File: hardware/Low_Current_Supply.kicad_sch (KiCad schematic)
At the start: 19 parts, among them U5001 TPS62160DSG, U5002 TPS73633DBVR

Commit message: feat(schematic): refactor main heirarchy
This commit makes a bunch of changes to how power is delivered on the
schematic. It also adds the probit header and the i2c output connector
on the main page of the schematic. Lastly, it changes it so that USB
power should work and also not power the 5V rail to the mosfet ICs.
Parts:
- added D5003: FIX ME PLEASE I BEG OF YOU, symbol Device:D
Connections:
- net at C5002.1, L5001.2, R5001.2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: now also D5003.2 (A); no longer C5003.1, R5003.1, TP5003.1, U5002.1 (IN), U5002.3 (EN)
- net 3.3V renamed +3.3V
- new net VBUS: C5003.1, D5003.1 (K), R5003.1, TP5003.1, U5002.1 (IN), U5002.3 (EN)
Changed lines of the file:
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@@
 	(paper "A4")
 	(junction
+		(at 144.78 71.12)
+		(diameter 0)
+		(color 0 0 0 0)
+	)
+	(junction
 		(at 191.77 113.03)
 		(diameter 0)
@@
 	)
 	(junction
+		(at 158.75 100.33)
+		(diameter 0)
+		(color 0 0 0 0)
+	)
+	(junction
+		(at 119.38 71.12)
+		(diameter 0)
+		(color 0 0 0 0)
+	)
+	(junction
+		(at 96.52 90.17)
+		(diameter 0)
+		(color 0 0 0 0)
+	)
+	(junction
+		(at 245.11 95.25)
+		(diameter 0)
+		(color 0 0 0 0)
+	)
+	(junction
+		(at 222.25 71.12)
+		(diameter 0)
+		(color 0 0 0 0)
+	)
+	(junction
+		(at 132.08 71.12)
+		(diameter 0)
+		(color 0 0 0 0)
+	)
+	(junction
+		(at 71.12 71.12)
+		(diameter 0)
+		(color 0 0 0 0)
+	)
+	(junction
+		(at 91.44 90.17)
+		(diameter 0)
+		(color 0 0 0 0)
+	)
+	(junction
+		(at 237.49 95.25)
+		(diameter 0)
+		(color 0 0 0 0)
+	)
+	(junction
+		(at 109.22 90.17)
+		(diameter 0)
+		(color 0 0 0 0)
+	)
+	(junction
+		(at 158.75 95.25)
+		(diameter 0)
+		(color 0 0 0 0)
+	)
+	(junction
+		(at 78.74 71.12)
+		(diameter 0)
+		(color 0 0 0 0)
+	)
+	(junction
 		(at 158.75 71.12)
 		(diameter 0)
@@
 	)
 	(junction
-		(at 158.75 100.33)
-		(diameter 0)
-		(color 0 0 0 0)
-	)
-	(junction
-		(at 119.38 71.12)
-		(diameter 0)
-		(color 0 0 0 0)
-	)
-	(junction
-		(at 96.52 90.17)
-		(diameter 0)
-		(color 0 0 0 0)
-	)
-	(junction
-		(at 245.11 95.25)
-		(diameter 0)
-		(color 0 0 0 0)
-	)
-	(junction
-		(at 222.25 71.12)
-		(diameter 0)
-		(color 0 0 0 0)
-	)
-	(junction
-		(at 132.08 71.12)
-		(diameter 0)
-		(color 0 0 0 0)
-	)
-	(junction
-		(at 71.12 71.12)
-		(diameter 0)
-		(color 0 0 0 0)
-	)
-	(junction
-		(at 91.44 90.17)
-		(diameter 0)
-		(color 0 0 0 0)
-	)
-	(junction
-		(at 237.49 95.25)
-		(diameter 0)
-		(color 0 0 0 0)
-	)
-	(junction
-		(at 109.22 90.17)
-		(diameter 0)
-		(color 0 0 0 0)
-	)
-	(junction
-		(at 158.75 95.25)
-		(diameter 0)
-		(color 0 0 0 0)
-	)
-	(junction
-		(at 78.74 71.12)
-		(diameter 0)
-		(color 0 0 0 0)
-	)
-	(junction
 		(at 194.31 71.12)
 		(diameter 0)
@@
 	)
 	(junction
-		(at 144.78 71.12)
-		(diameter 0)
-		(color 0 0 0 0)
-	)
-	(junction
 		(at 261.62 95.25)
 		(diameter 0)
@@
 	(wire
 		(pts
-			(xy 144.78 71.12) (xy 158.75 71.12)
-		)
-		(stroke
-			(width 0)
-			(type default)
-		)
-	)
-	(wire
-		(pts
 			(xy 237.49 95.25) (xy 245.11 95.25)
 		)
@@
 	(wire
 		(pts
+			(xy 144.78 71.12) (xy 147.32 71.12)
+		)
+		(stroke
+			(width 0)
+			(type default)
+		)
+	)
+	(wire
+		(pts
 			(xy 222.25 71.12) (xy 270.51 71.12)
 		)
@@
 	(wire
 		(pts
+			(xy 158.75 62.23) (xy 158.75 71.12)
+		)
+		(stroke
+			(width 0)
+			(type default)
+		)
+	)
+	(wire
+		(pts
 			(xy 223.52 95.25) (xy 228.6 95.25)
 		)
@@
 	(wire
 		(pts
+			(xy 154.94 71.12) (xy 158.75 71.12)
+		)
+		(stroke
+			(width 0)
+			(type default)
+		)
+	)
+	(wire
+		(pts
 			(xy 91.44 90.17) (xy 91.44 88.9)
 		)
@@
 		)
 	)
-	(global_label "5V"
+	(hierarchical_label "VBUS"
 		(shape input)
-		(at 270.51 71.12 0)
-		(fields_autoplaced yes)
+		(at 158.75 62.23 180)
 		(effects
 			(font
 				(size 1.27 1.27)
 			)
-			(justify left)
-		)
-		(property "Intersheetrefs" "${INTERSHEET_REFS}"
-			(at 275.7933 71.12 0)
-			(effects
-				(font
-					(size 1.27 1.27)
-				)
-				(justify left)
-				(hide yes)
-			)
-		)
-	)
-	(global_label "12V"
+			(justify right)
+		)
+	)
+	(hierarchical_label "12V"
 		(shape input)
 		(at 46.99 71.12 180)
-		(fields_autoplaced yes)
 		(effects
 			(font
@@
 			(justify right)
 		)
-		(property "Intersheetrefs" "${INTERSHEET_REFS}"
-			(at 40.4972 71.12 0)
-			(effects
-				(font
-					(size 1.27 1.27)
-				)
-				(justify right)
-				(hide yes)
-			)
-		)
-	)
-	(global_label "3.3V"
-		(shape input)
+	)
+	(hierarchical_label "+3.3V"
+		(shape output)
 		(at 269.24 95.25 0)
-		(fields_autoplaced yes)
 		(effects
 			(font
@@
 			(justify left)
 		)
-		(property "Intersheetrefs" "${INTERSHEET_REFS}"
-			(at 276.3376 95.25 0)
-			(effects
-				(font
-					(size 1.27 1.27)
-				)
-				(justify left)
-				(hide yes)
-			)
+	)
+	(hierarchical_label "5V"
+		(shape output)
+		(at 270.51 71.12 0)
+		(effects
+			(font
+				(size 1.27 1.27)
+			)
+			(justify left)
 		)
 	)
@@
 					(unit 1)
 				)
+			)
+		)
+	)
+	(symbol
+		(lib_id "Device:D")
+		(at 151.13 71.12 180)
+		(unit 1)
+		(exclude_from_sim no)
+		(in_bom yes)
+		(on_board yes)
+		(dnp no)
+		(fields_autoplaced yes)
+		(property "Reference" "D5003"
+			(at 151.13 64.77 0)
+			(effects
+				(font
+					(size 1.27 1.27)
+				)
+			)
+		)
+		(property "Value" "FIX ME PLEASE I BEG OF YOU"
+			(at 151.13 67.31 0)
+			(effects
+				(font
+					(size 1.27 1.27)
+				)
+			)
+		)
+		(property "Footprint" ""
+			(at 151.13 71.12 0)
+			(effects
+				(font
+					(size 1.27 1.27)
+				)
+				(hide yes)
+			)
+		)
+		(property "Datasheet" "~"
+			(at 151.13 71.12 0)
+			(effects
+				(font
+					(size 1.27 1.27)
+				)
+				(hide yes)
+			)
+		)
+		(property "Description" "Diode"
+			(at 151.13 71.12 0)
+			(effects
+				(font
+					(size 1.27 1.27)
+				)
+				(hide yes)
+			)
+		)
+		(property "Sim.Device" "D"
+			(at 151.13 71.12 0)
+			(effects
+				(font
+					(size 1.27 1.27)
+				)
+				(hide yes)
+			)
+		)
+		(property "Sim.Pins" "1=K 2=A"
+			(at 151.13 71.12 0)
+			(effects
+				(font
+					(size 1.27 1.27)
+				)
+				(hide yes)
+			)
+		)
+		(pin "1"
+		)
+		(pin "2"
+		)
+		(instances
+			(project ""
+				(path "/d5303413-7068-41ba-88e3-39dfa38d31b7/c1da4524-645b-40e4-93f8-f7b345299022"
+					(reference "D5003")
+					(unit 1)
+				)

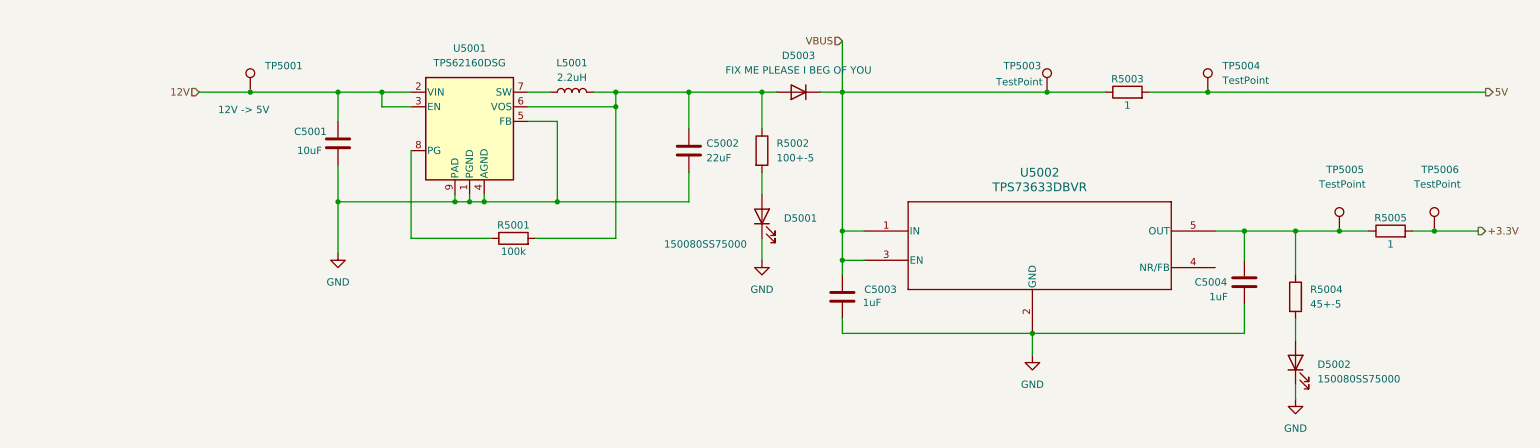
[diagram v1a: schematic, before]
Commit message: feat: fix pcb changes for 12V and low current supply
Swapped 5V regulator, added diodes, fixed connectors and general
placement. Changes to complete list for 12V and low current supply.
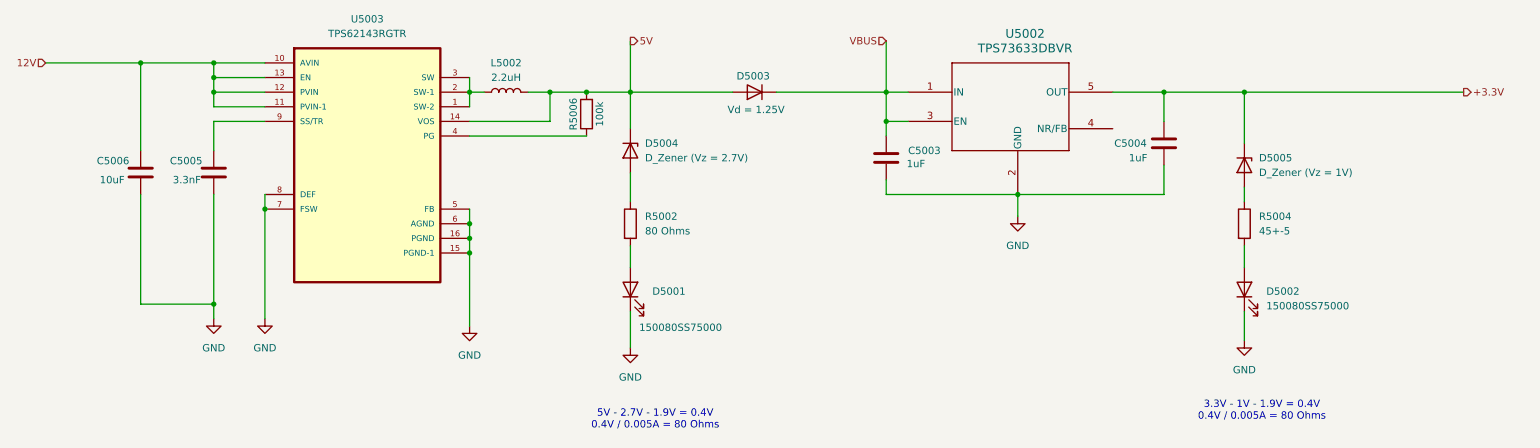
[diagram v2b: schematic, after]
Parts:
- removed C5001: 10uF, Capacitor_SMD:C_0805_2012Metric_Pad1.18x1.45mm_HandSolder, symbol Device:C
- removed C5002: 22uF, Capacitor_SMD:C_0805_2012Metric, symbol Device:C
- removed L5001: 2.2uH, Inductor_SMD:L_0805_2012Metric_Pad1.15x1.40mm_HandSolder, symbol Device:L
- removed R5001: 100k, Resistor_SMD:R_0805_2012Metric, symbol Device:R
- removed R5003, R5005: 1, Resistor_SMD:R_0805_2012Metric, symbol Device:R
- removed TP5001: 12V -> 5V, TestPoint:TestPoint_Pad_1.5x1.5mm, symbol Connector:TestPoint
- removed TP5003, TP5004, TP5005, TP5006: TestPoint, TestPoint:TestPoint_Pad_1.5x1.5mm, symbol Connector:TestPoint
- removed U5001: TPS62160DSG, Package_SON:WSON-8-1EP_2x2mm_P0.5mm_EP0.9x1.6mm_ThermalVias, symbol Regulator_Switching:TPS62160DSG
- added C5005: 3.3nF, Capacitor_SMD:C_0805_2012Metric_Pad1.18x1.45mm_HandSolder, symbol Device:C
- added C5006: 10uF, Capacitor_SMD:C_0805_2012Metric_Pad1.18x1.45mm_HandSolder, symbol Device:C
- added D5004: D_Zener (Vz = 2.7V), work:SOD123_DIO, symbol Device:D_Zener
- added D5005: D_Zener (Vz = 1V), work:P25_DO-214AC_SMA, symbol Device:D_Zener
- added L5002: 2.2uH, Inductor_SMD:L_0805_2012Metric_Pad1.15x1.40mm_HandSolder, symbol Device:L
- added R5006: 100k, Resistor_SMD:R_0805_2012Metric, symbol Device:R
- added U5003: TPS62143RGTR, TPS62143RGTR:QFN50P300X300X100-17N, symbol TPS62143RGTR:TPS62143RGTR
- D5003: value FIX ME PLEASE I BEG OF YOU -> Vd = 1.25V; footprint (none) -> work:SOD123_DIO
- R5002: value 100+-5 -> 80 Ohms
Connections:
- net +3.3V: now also C5004.1, U5002.5 (OUT), D5005.1 (K)
- net 12V: now also C5006.1, U5003.10 (AVIN), U5003.11 (PVIN-1), U5003.12 (PVIN), U5003.13 (EN)
- net 5V: now also D5003.2 (A), D5004.1 (K), L5002.2, R5006.2, U5003.14 (VOS)
- net GND: now also C5005.2, C5006.2, U5003.15 (PGND-1), U5003.16 (PGND), U5003.5 (FB), U5003.6 (AGND), U5003.7 (FSW), U5003.8 (DEF)
- net at R5002.1: now also D5004.2 (A); no longer D5003.2 (A)
- new net: L5002.1, U5003.1 (SW-2), U5003.2 (SW-1), U5003.3 (SW)
- new net: R5006.1, U5003.4 (PG)
- new net: C5005.1, U5003.9 (SS/TR)
- new net: D5005.2 (A), R5004.1
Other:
- note added: "3.3V - 1V - 1.9V = 0.4V 0.4V / 0.005A = 80 Ohms"
- note added: "5V - 2.7V - 1.9V = 0.4V 0.4V / 0.005A = 80 Ohms"
- moved on the sheet: C5003, C5004, D5001, D5002, D5003, R5002, R5004, U5002

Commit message: feat(schematic): added cooler mounting holes
added cooler mounting holes to schematic
changed temp pins to read proper tempurature
small fixes
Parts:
- C5003, C5004: footprint Capacitor_SMD:C_0805_2012Metric -> Capacitor_SMD:C_0402_1005Metric
- C5005: footprint Capacitor_SMD:C_0805_2012Metric_Pad1.18x1.45mm_HandSolder -> Capacitor_SMD:C_0402_1005Metric
- C5006: footprint Capacitor_SMD:C_0805_2012Metric_Pad1.18x1.45mm_HandSolder -> Capacitor_SMD:C_0603_1608Metric
- D5001, D5002: footprint LED_SMD:LED_0805_2012Metric_Pad1.15x1.40mm_HandSolder -> LED_SMD:LED_0603_1608Metric
- L5002: footprint Inductor_SMD:L_0805_2012Metric_Pad1.15x1.40mm_HandSolder -> work:IND-SMD_L7.2-W6.6_GPSR07X0
- R5002: value 80 Ohms -> 82
- R5004: value 45+-5 -> 82
- R5006: footprint Resistor_SMD:R_0805_2012Metric -> Resistor_SMD:R_0402_1005Metric
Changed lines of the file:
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@@
 		(shape input)
 		(at 166.37 62.23 180)
-		(fields_autoplaced yes)
 		(effects
 			(font
@@
 		(shape input)
 		(at 20.32 66.04 180)
-		(fields_autoplaced yes)
 		(effects
 			(font
@@
 		(shape output)
 		(at 266.7 71.12 0)
-		(fields_autoplaced yes)
 		(effects
 			(font
@@
 		(shape output)
 		(at 121.92 62.23 0)
-		(fields_autoplaced yes)
 		(effects
 			(font
@@
 			)
 		)
-		(property "Datasheet" ""
+		(property "Datasheet" "https://jlcpcb.com/partdetail/TexasInstruments-TPS62143RGTR/C2070702"
 			(at 76.2 83.82 0)
 			(effects
@@
 			)
 		)
-		(property "Footprint" "LED_SMD:LED_0805_2012Metric_Pad1.15x1.40mm_HandSolder"
+		(property "Footprint" "LED_SMD:LED_0603_1608Metric"
 			(at 228.6 105.41 0)
 			(effects
@@
 			)
 		)
-		(property "Datasheet" "~"
+		(property "Datasheet" "https://jlcpcb.com/partdetail/Hubei_KentoElec-KT0603R/C2286"
 			(at 228.6 105.41 0)
 			(effects
@@
 			)
 		)
-		(property "Value" "80 Ohms"
+		(property "Value" "82"
 			(at 124.46 95.2499 0)
 			(effects
@@
 			)
 		)
-		(property "Datasheet" "~"
+		(property "Datasheet" "https://jlcpcb.com/partdetail/18529-0805W8F820JT5E/C17841"
 			(at 121.92 93.98 0)
 			(effects
@@
 			)
 		)
-		(property "Footprint" "Capacitor_SMD:C_0805_2012Metric_Pad1.18x1.45mm_HandSolder"
+		(property "Footprint" "Capacitor_SMD:C_0402_1005Metric"
 			(at 50.4952 88.9 0)
 			(effects
@@
 			)
 		)
-		(property "Datasheet" "~"
+		(property "Datasheet" "https://jlcpcb.com/partdetail/1888-0402B332K500NT/C1536"
 			(at 49.53 85.09 0)
 			(effects
@@
 			)
 		)
-		(property "Datasheet" "TPS73633DBVR"
+		(property "Datasheet" "https://jlcpcb.com/partdetail/TexasInstruments-TPS73633DBVR/C28038"
 			(at 160.02 71.12 0)
 			(effects
@@
 			)
 		)
-		(property "Footprint" "Capacitor_SMD:C_0805_2012Metric"
+		(property "Footprint" "Capacitor_SMD:C_0402_1005Metric"
 			(at 167.3352 86.36 0)
 			(effects
@@
 			)
 		)
-		(property "Datasheet" "~"
+		(property "Datasheet" "https://jlcpcb.com/partdetail/15107-CL05A105KP5NNNC/C14445"
 			(at 166.37 82.55 0)
 			(effects
@@
 			)
 		)
-		(property "Footprint" "Resistor_SMD:R_0805_2012Metric"
+		(property "Footprint" "Resistor_SMD:R_0402_1005Metric"
 			(at 116.078 74.93 90)
 			(effects
@@
 			)
 		)
-		(property "Datasheet" "~"
+		(property "Datasheet" "https://jlcpcb.com/partdetail/26484-0402WGF1003TCE/C25741"
 			(at 114.3 74.93 0)
 			(effects
@@
 			)
 		)
-		(property "Value" "45+-5"
+		(property "Value" "82"
 			(at 231.14 95.2499 0)
 			(effects
@@
 			)
 		)
-		(property "Datasheet" "~"
+		(property "Datasheet" "https://jlcpcb.com/partdetail/18529-0805W8F820JT5E/C17841"
 			(at 228.6 93.98 0)
 			(effects
@@
 			)
 		)
-		(property "Footprint" "Capacitor_SMD:C_0805_2012Metric_Pad1.18x1.45mm_HandSolder"
+		(property "Footprint" "Capacitor_SMD:C_0603_1608Metric"
 			(at 37.7952 88.9 0)
 			(effects
@@
 			)
 		)
-		(property "Datasheet" "~"
+		(property "Datasheet" "https://jlcpcb.com/partdetail/71320-0603X106K160NT/C70225"
 			(at 36.83 85.09 0)
 			(effects
@@
 			)
 		)
-		(property "Footprint" "LED_SMD:LED_0805_2012Metric_Pad1.15x1.40mm_HandSolder"
+		(property "Footprint" "LED_SMD:LED_0603_1608Metric"
 			(at 121.92 105.41 0)
 			(effects
@@
 			)
 		)
-		(property "Datasheet" "~"
+		(property "Datasheet" "https://jlcpcb.com/partdetail/Hubei_KentoElec-KT0603R/C2286"
 			(at 121.92 105.41 0)
 			(effects
@@
 			)
 		)
-		(property "Footprint" "Inductor_SMD:L_0805_2012Metric_Pad1.15x1.40mm_HandSolder"
+		(property "Footprint" "work:IND-SMD_L7.2-W6.6_GPSR07X0"
 			(at 100.33 71.12 0)
 			(effects
@@
 			)
 		)
-		(property "Datasheet" "~"
+		(property "Datasheet" "https://jlcpcb.com/partdetail/ShouHan-CYA0630_22UH/C5189746"
 			(at 100.33 71.12 0)
 			(effects
@@
 			)
 		)
-		(property "Footprint" "Capacitor_SMD:C_0805_2012Metric"
+		(property "Footprint" "Capacitor_SMD:C_0402_1005Metric"
 			(at 215.5952 83.82 0)
 			(effects
@@
 			)
 		)
-		(property "Datasheet" "~"
+		(property "Datasheet" "https://jlcpcb.com/partdetail/15107-CL05A105KP5NNNC/C14445"
 			(at 214.63 80.01 0)
 			(effects

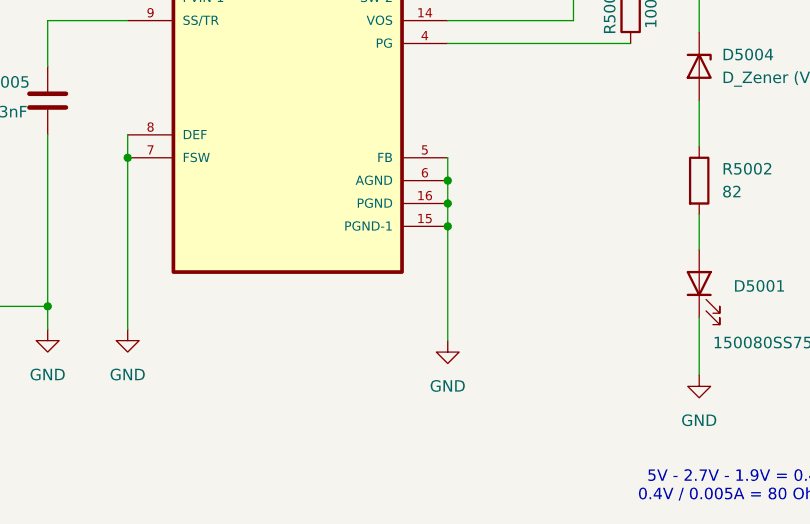
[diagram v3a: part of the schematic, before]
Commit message: feat(hardware): microcontroller routing
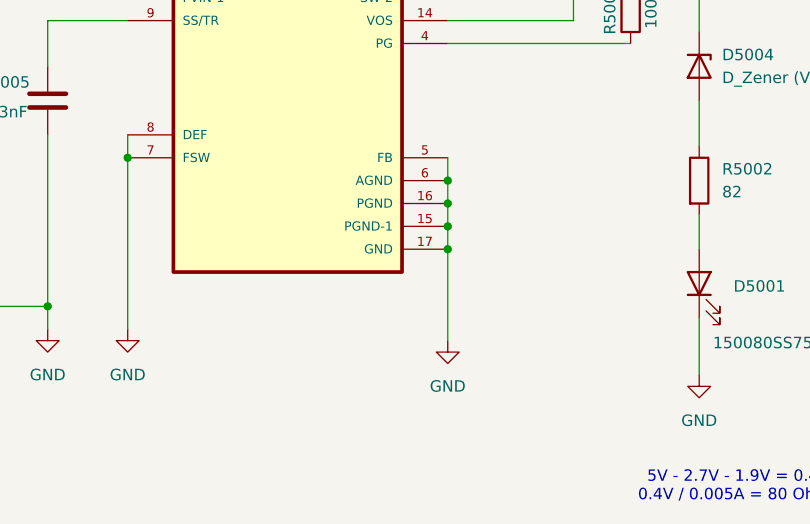
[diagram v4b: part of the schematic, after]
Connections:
- net GND: now also U5003.17 (GND), U5003.18 (GND), U5003.19 (GND), U5003.20 (GND), U5003.21 (GND), U5003.22 (GND)
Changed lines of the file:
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@@
+	)
+	(junction
+		(at 93.98 101.6)
+		(diameter 0)
+		(color 0 0 0 0)
 	)
 	(junction
@@
 	(wire
 		(pts
-			(xy 93.98 99.06) (xy 93.98 111.76)
+			(xy 93.98 99.06) (xy 93.98 101.6)
 		)
 		(stroke
@@
 		(pts
 			(xy 104.14 71.12) (xy 107.95 71.12)
+		)
+		(stroke
+			(width 0)
+			(type default)
+		)
+	)
+	(wire
+		(pts
+			(xy 93.98 101.6) (xy 93.98 111.76)
 		)
 		(stroke
@@
 		(pin "6"
 		)
+		(pin "18"
+		)
+		(pin "17"
+		)
+		(pin "22"
+		)
+		(pin "21"
+		)
+		(pin "20"
+		)
+		(pin "19"
+		)
 		(instances

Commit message: chore(schematic): add LCSC Part Numbers
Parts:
- C5003, C5004: LCSC Part Number (none) -> C14445
- C5005: LCSC Part Number (none) -> C1536
- C5006: LCSC Part Number (none) -> C70225
- D5001, D5002: LCSC Part Number (none) -> C2286
- L5002: LCSC Part Number (none) -> C5189746
- R5002, R5004: LCSC Part Number (none) -> C17841
- R5006: LCSC Part Number (none) -> C25741
- U5002: LCSC Part Number (none) -> C28038
- U5003: LCSC Part Number (none) -> C2070702
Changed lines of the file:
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@@
+			)
+		)
+		(property "LCSC Part Number" "C2070702"
+			(at 76.2 83.82 0)
+			(effects
+				(font
+					(size 1.27 1.27)
+				)
+				(hide yes)
 			)
 		)
@@
 			)
 		)
+		(property "LCSC Part Number" "C2286"
+			(at 228.6 105.41 0)
+			(effects
+				(font
+					(size 1.27 1.27)
+				)
+				(hide yes)
+			)
+		)
 		(pin "2"
 		)
@@
 			)
 		)
+		(property "LCSC Part Number" ""
+			(at 121.92 81.28 0)
+			(effects
+				(font
+					(size 1.27 1.27)
+				)
+				(hide yes)
+			)
+		)
 		(pin "2"
 		)
@@
 		)
 		(property "Sim.Pins" "1=K 2=A"
+			(at 143.51 71.12 0)
+			(effects
+				(font
+					(size 1.27 1.27)
+				)
+				(hide yes)
+			)
+		)
+		(property "LCSC Part Number" ""
 			(at 143.51 71.12 0)
 			(effects
@@
 			)
 		)
+		(property "LCSC Part Number" "C17841"
+			(at 121.92 93.98 0)
+			(effects
+				(font
+					(size 1.27 1.27)
+				)
+				(hide yes)
+			)
+		)
 		(pin "2"
 		)
@@
 			)
 		)
+		(property "LCSC Part Number" "C1536"
+			(at 49.53 85.09 0)
+			(effects
+				(font
+					(size 1.27 1.27)
+				)
+				(hide yes)
+			)
+		)
 		(pin "2"
 		)
@@
 			)
 		)
+		(property "LCSC Part Number" "C28038"
+			(at 160.02 71.12 0)
+			(effects
+				(font
+					(size 1.27 1.27)
+				)
+				(hide yes)
+			)
+		)
 		(pin "4"
 		)
@@
 			)
 		)
+		(property "LCSC Part Number" "C14445"
+			(at 166.37 82.55 0)
+			(effects
+				(font
+					(size 1.27 1.27)
+				)
+				(hide yes)
+			)
+		)
 		(pin "2"
 		)
@@
 		)
 		(property "Description" "Resistor"
+			(at 114.3 74.93 0)
+			(effects
+				(font
+					(size 1.27 1.27)
+				)
+				(hide yes)
+			)
+		)
+		(property "LCSC Part Number" "C25741"
 			(at 114.3 74.93 0)
 			(effects
@@
 			)
 		)
+		(property "LCSC Part Number" "C17841"
+			(at 228.6 93.98 0)
+			(effects
+				(font
+					(size 1.27 1.27)
+				)
+				(hide yes)
+			)
+		)
 		(pin "2"
 		)
@@
 		)
 		(property "Description" "Unpolarized capacitor"
+			(at 36.83 85.09 0)
+			(effects
+				(font
+					(size 1.27 1.27)
+				)
+				(hide yes)
+			)
+		)
+		(property "LCSC Part Number" "C70225"
 			(at 36.83 85.09 0)
 			(effects
@@
 			)
 		)
+		(property "LCSC Part Number" "C2286"
+			(at 121.92 105.41 0)
+			(effects
+				(font
+					(size 1.27 1.27)
+				)
+				(hide yes)
+			)
+		)
 		(pin "2"
 		)
@@
 			)
 		)
+		(property "LCSC Part Number" "C5189746"
+			(at 100.33 71.12 0)
+			(effects
+				(font
+					(size 1.27 1.27)
+				)
+				(hide yes)
+			)
+		)
 		(pin "1"
 		)
@@
 		)
 		(property "Description" "Unpolarized capacitor"
+			(at 214.63 80.01 0)
+			(effects
+				(font
+					(size 1.27 1.27)
+				)
+				(hide yes)
+			)
+		)
+		(property "LCSC Part Number" "C14445"
 			(at 214.63 80.01 0)
 			(effects
@@
 			(at 228.6 83.82 0)
 			(effects
+				(font
+					(size 1.27 1.27)
+				)
+				(hide yes)
+			)
+		)
+		(property "LCSC Part Number" ""
+			(at 228.6 83.82 0)
+			(effects
